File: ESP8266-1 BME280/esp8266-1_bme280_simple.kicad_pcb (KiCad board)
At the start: 2 copper layers, 21.6 x 15.6 mm, 12 parts, among them J1 USB_B_Micro, J2 Conn_02x04_Odd_Even, SW1 SW_DIP_x01, U1 AMS1117-3.3, U2 BME280

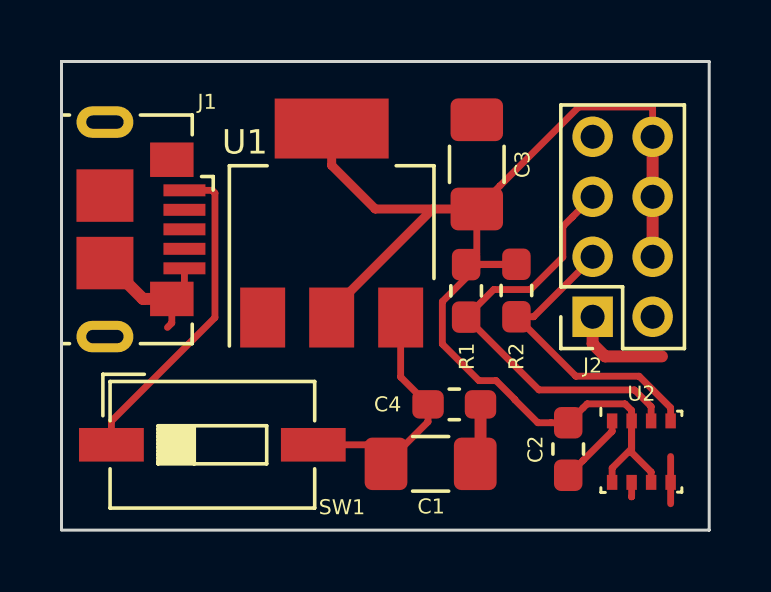
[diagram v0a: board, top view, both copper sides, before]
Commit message: Remove power switch, final design v0.1.0
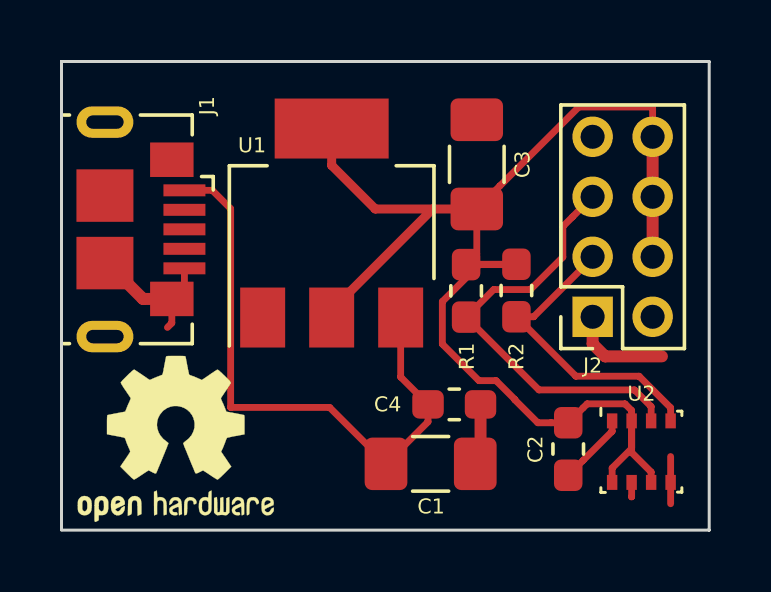
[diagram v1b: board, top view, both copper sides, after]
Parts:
- removed SW1: SW_DIP_x01, Button_Switch_SMD:SW_DIP_SPSTx01_Slide_6.7x4.1mm_W6.73mm_P2.54mm_LowProfile_JPin
- C1, C3: value 10uF -> 10 uF
- C2, C4: value 100nF -> 100 nF
- REF**: moved to F.Cu
- moved REF** 8.71 mm to (114.0, 98.4), turned to 0 degrees
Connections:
- J1 pad 1: Net-(J1-Pad1) -> Net-(C1-Pad1)
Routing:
- net Net-(C1-Pad1): track 9.16 -> 20.9 mm
- net Net-(J1-Pad1): track 10.9 -> 0.00 mm
